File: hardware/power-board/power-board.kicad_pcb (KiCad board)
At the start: 2 copper layers, 60 x 105 mm, 15 parts, among them J1 Screw_Terminal_01x02, J2 Screw_Terminal_01x08, J3 Screw_Terminal_01x08, U1 TSR_1-2433, U2 TSR_1-2450

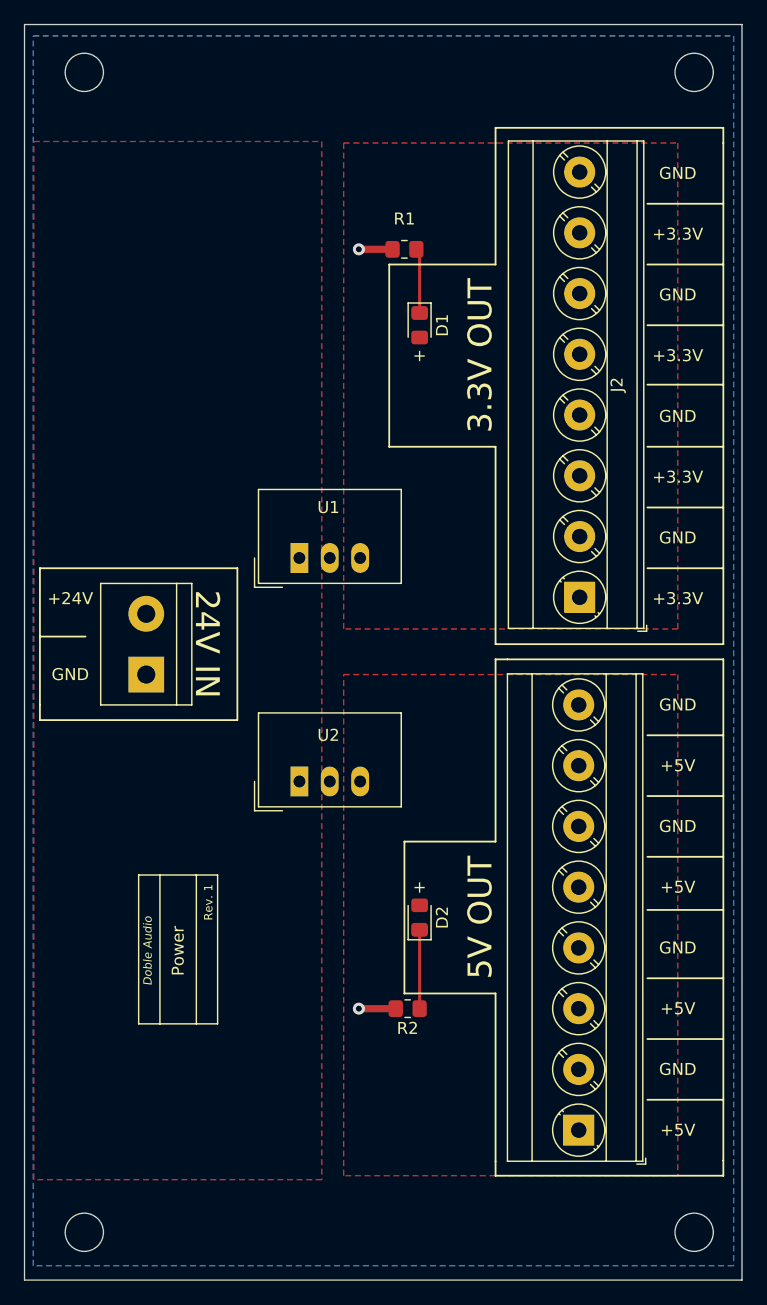
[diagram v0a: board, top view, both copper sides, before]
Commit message: Smaller board
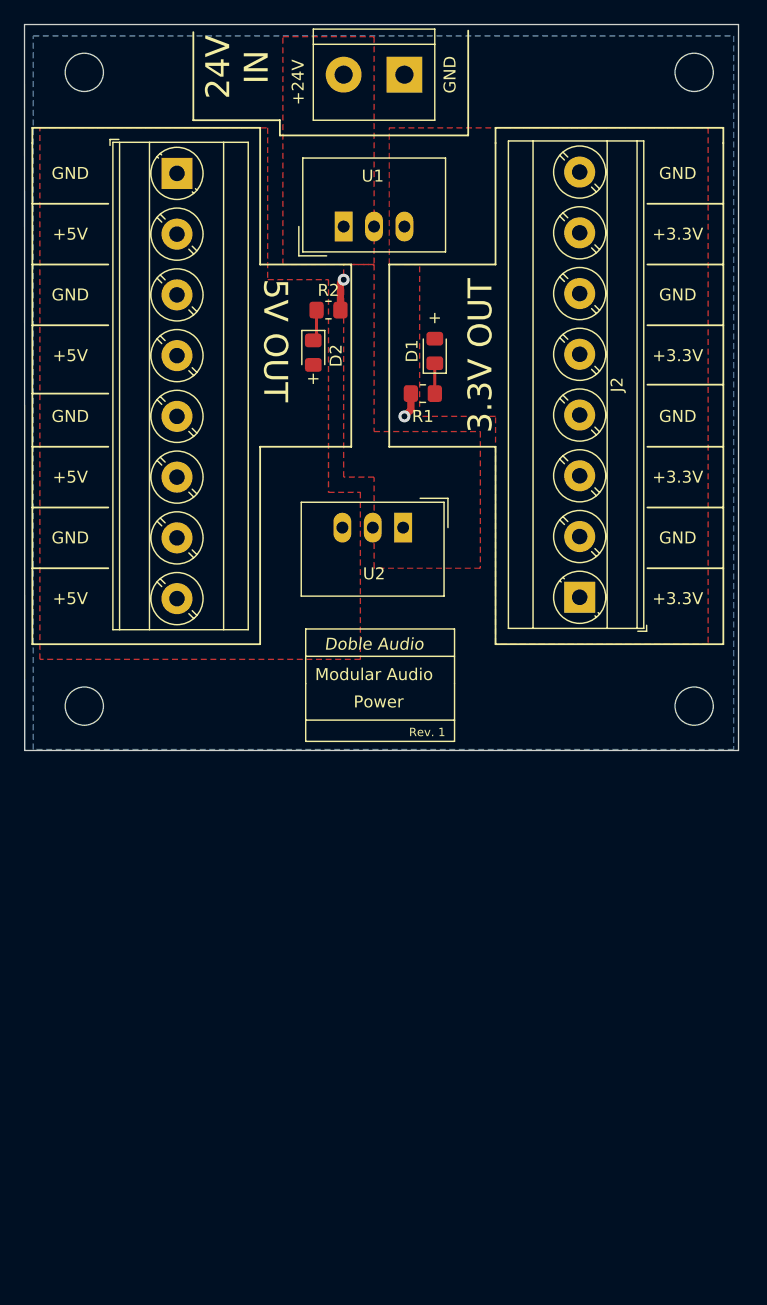
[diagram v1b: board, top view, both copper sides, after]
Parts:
- moved J3 86.8 mm to (45.8, 44.5), turned to -90 degrees
- moved R2 58.8 mm to (58.4, 55.9), turned to 0 degrees
- moved J1 54.6 mm to (64.8, 36.2), turned to 180 degrees
- moved D2 48.1 mm to (57.1, 59.4), turned to -90 degrees
- moved REF** 44.0 mm to (38.0, 89.0)
- moved REF** 44.0 mm to (89.0, 89.0)
- moved REF** 40.9 mm to (74.9, 86.4)
- moved REF** 29.4 mm to (48.3, 87.6)
- moved U1 28.0 mm to (59.7, 48.9)
- moved U2 22.9 mm to (64.7, 74.1), turned to 180 degrees
- moved R1 12.2 mm to (66.3, 62.9)
- moved D1 2.50 mm to (67.3, 59.3), turned to 90 degrees
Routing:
- net Net-(D2-Pad1): track 6.59 -> 2.65 mm
- net Net-(D1-Pad1): track 5.44 -> 2.54 mm
- net GND: track 5.89 -> 4.78 mm
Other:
- board size 60 x 105 mm -> 59.7 x 60.7 mm
- board text added: "Modular Audio"
